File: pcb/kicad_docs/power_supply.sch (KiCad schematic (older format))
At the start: 32 parts, among them J5 power_in, U7 AMS1117-3.3

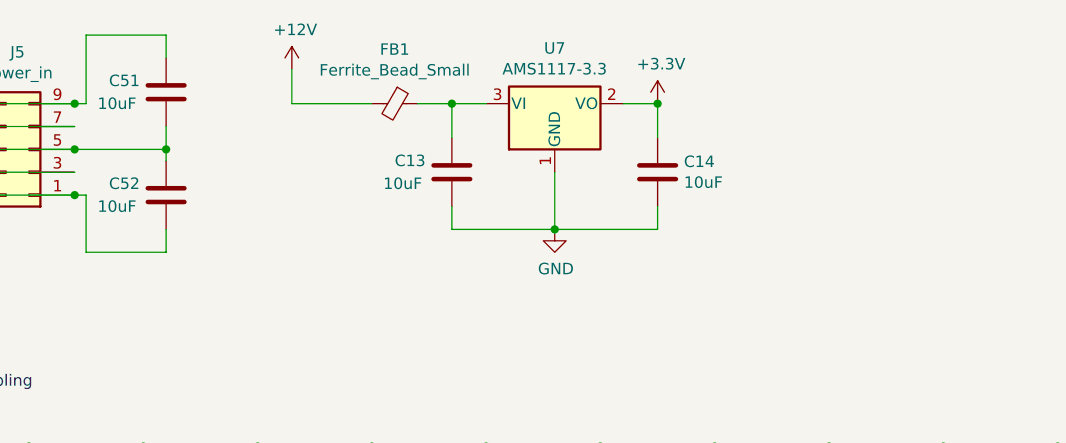
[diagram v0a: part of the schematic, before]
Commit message: add title blocks, fix some erc violations
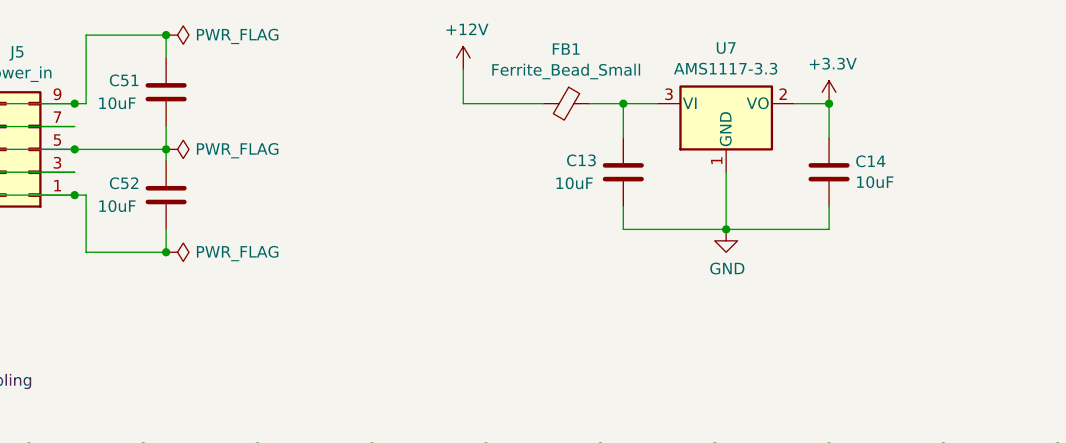
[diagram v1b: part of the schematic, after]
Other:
- moved on the sheet: C13, C14, FB1, U7
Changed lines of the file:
@@
 encoding utf-8
 Sheet 5 10
-Title ""
-Date ""
-Rev ""
+Title "Quad ADSR"
+Date "2020-07-31"
+Rev "0"
 Comp ""
-Comment1 ""
-Comment2 ""
-Comment3 ""
+Comment1 "creativecommons.org/licenses/by/4.0/"
+Comment2 "License: CC by 4.0"
+Comment3 "Author: Jordan Aceto"
 Comment4 ""
 $EndDescr
@@
 L power:GND #PWR045
 U 1 1 5EE07C6F
-P 3800 1550
-F 0 "#PWR045" H 3800 1300 50  0001 C CNN
-F 1 "GND" H 3805 1377 50  0000 C CNN
-F 2 "" H 3800 1550 50  0001 C CNN
-F 3 "" H 3800 1550 50  0001 C CNN
-	1    3800 1550
-	1    0    0    -1
-$EndComp
-Connection ~ 4250 1000
+P 4550 1550
+F 0 "#PWR045" H 4550 1300 50  0001 C CNN
+F 1 "GND" H 4555 1377 50  0000 C CNN
+F 2 "" H 4550 1550 50  0001 C CNN
+F 3 "" H 4550 1550 50  0001 C CNN
+	1    4550 1550
+	1    0    0    -1
+$EndComp
+Connection ~ 5000 1000
 $Comp
 L power:+3.3V #PWR046
 U 1 1 5EE05D61
-P 4250 1000
-F 0 "#PWR046" H 4250 850 50  0001 C CNN
-F 1 "+3.3V" H 4265 1173 50  0000 C CNN
-F 2 "" H 4250 1000 50  0001 C CNN
-F 3 "" H 4250 1000 50  0001 C CNN
-	1    4250 1000
-	1    0    0    -1
-$EndComp
-Wire Wire Line
-	2650 1000 3000 1000
-Wire Wire Line
-	2650 1000 2650 850
+P 5000 1000
+F 0 "#PWR046" H 5000 850 50  0001 C CNN
+F 1 "+3.3V" H 5015 1173 50  0000 C CNN
+F 2 "" H 5000 1000 50  0001 C CNN
+F 3 "" H 5000 1000 50  0001 C CNN
+	1    5000 1000
+	1    0    0    -1
+$EndComp
+Wire Wire Line
+	3400 1000 3750 1000
+Wire Wire Line
+	3400 1000 3400 850
 $Comp
 L power:+12V #PWR044
 U 1 1 5EE0026F
-P 2650 850
-F 0 "#PWR044" H 2650 700 50  0001 C CNN
-F 1 "+12V" H 2665 1023 50  0000 C CNN
-F 2 "" H 2650 850 50  0001 C CNN
-F 3 "" H 2650 850 50  0001 C CNN
-	1    2650 850
-	1    0    0    -1
-$EndComp
-Wire Wire Line
-	3800 1550 4250 1550
-Connection ~ 3800 1550
-Wire Wire Line
-	3800 1300 3800 1550
-Wire Wire Line
-	4250 1550 4250 1450
-Wire Wire Line
-	3350 1550 3800 1550
-Wire Wire Line
-	3350 1450 3350 1550
-Wire Wire Line
-	4250 1000 4100 1000
-Wire Wire Line
-	4250 1150 4250 1000
-Wire Wire Line
-	3350 1000 3500 1000
-Connection ~ 3350 1000
-Wire Wire Line
-	3350 1150 3350 1000
-Wire Wire Line
-	3200 1000 3350 1000
+P 3400 850
+F 0 "#PWR044" H 3400 700 50  0001 C CNN
+F 1 "+12V" H 3415 1023 50  0000 C CNN
+F 2 "" H 3400 850 50  0001 C CNN
+F 3 "" H 3400 850 50  0001 C CNN
+	1    3400 850
+	1    0    0    -1
+$EndComp
+Wire Wire Line
+	4550 1550 5000 1550
+Connection ~ 4550 1550
+Wire Wire Line
+	4550 1300 4550 1550
+Wire Wire Line
+	5000 1550 5000 1450
+Wire Wire Line
+	4100 1550 4550 1550
+Wire Wire Line
+	4100 1450 4100 1550
+Wire Wire Line
+	5000 1000 4850 1000
+Wire Wire Line
+	5000 1150 5000 1000
+Wire Wire Line
+	4100 1000 4250 1000
+Connection ~ 4100 1000
+Wire Wire Line
+	4100 1150 4100 1000
+Wire Wire Line
+	3950 1000 4100 1000
 $Comp
 L Device:Ferrite_Bead_Small FB1
 U 1 1 5EDEC41C
-P 3100 1000
-F 0 "FB1" V 2863 1000 50  0000 C CNN
-F 1 "Ferrite_Bead_Small" V 2954 1000 50  0000 C CNN
-F 2 "Inductor_SMD:L_0805_2012Metric" V 3030 1000 50  0001 C CNN
-F 3 "~" H 3100 1000 50  0001 C CNN
-	1    3100 1000
+P 3850 1000
+F 0 "FB1" V 3613 1000 50  0000 C CNN
+F 1 "Ferrite_Bead_Small" V 3704 1000 50  0000 C CNN
+F 2 "Inductor_SMD:L_0805_2012Metric" V 3780 1000 50  0001 C CNN
+F 3 "~" H 3850 1000 50  0001 C CNN
+	1    3850 1000
 	0    1    1    0
 $EndComp
@@
 L Device:C C14
 U 1 1 5EDEAF58
-P 4250 1300
-F 0 "C14" H 4365 1346 50  0000 L CNN
-F 1 "10uF" H 4365 1255 50  0000 L CNN
-F 2 "Capacitor_SMD:C_0805_2012Metric" H 4288 1150 50  0001 C CNN
-F 3 "~" H 4250 1300 50  0001 C CNN
-	1    4250 1300
+P 5000 1300
+F 0 "C14" H 5115 1346 50  0000 L CNN
+F 1 "10uF" H 5115 1255 50  0000 L CNN
+F 2 "Capacitor_SMD:C_0805_2012Metric" H 5038 1150 50  0001 C CNN
+F 3 "~" H 5000 1300 50  0001 C CNN
+	1    5000 1300
 	1    0    0    -1
 $EndComp
@@
 L Device:C C13
 U 1 1 5EDEA933
-P 3350 1300
-F 0 "C13" H 3100 1350 50  0000 L CNN
-F 1 "10uF" H 3050 1250 50  0000 L CNN
-F 2 "Capacitor_SMD:C_1206_3216Metric" H 3388 1150 50  0001 C CNN
-F 3 "~" H 3350 1300 50  0001 C CNN
-	1    3350 1300
+P 4100 1300
+F 0 "C13" H 3850 1350 50  0000 L CNN
+F 1 "10uF" H 3800 1250 50  0000 L CNN
+F 2 "Capacitor_SMD:C_1206_3216Metric" H 4138 1150 50  0001 C CNN
+F 3 "~" H 4100 1300 50  0001 C CNN
+	1    4100 1300
 	1    0    0    -1
 $EndComp
@@
 L Regulator_Linear:AMS1117-3.3 U7
 U 1 1 5EDEA43C
-P 3800 1000
-F 0 "U7" H 3800 1242 50  0000 C CNN
-F 1 "AMS1117-3.3" H 3800 1151 50  0000 C CNN
-F 2 "Package_TO_SOT_SMD:SOT-223-3_TabPin2" H 3800 1200 50  0001 C CNN
-F 3 "http://www.advanced-monolithic.com/pdf/ds1117.pdf" H 3900 750 50  0001 C CNN
-	1    3800 1000
+P 4550 1000
+F 0 "U7" H 4550 1242 50  0000 C CNN
+F 1 "AMS1117-3.3" H 4550 1151 50  0000 C CNN
+F 2 "Package_TO_SOT_SMD:SOT-223-3_TabPin2" H 4550 1200 50  0001 C CNN
+F 3 "http://www.advanced-monolithic.com/pdf/ds1117.pdf" H 4650 750 50  0001 C CNN
+	1    4550 1000
 	1    0    0    -1
 $EndComp
@@
 Text Notes 900  6650 0    50   ~ 0
 24LCxx EEPROM decoupling
+$Comp
+L power:PWR_FLAG #FLG0101
+U 1 1 5F24F24E
+P 2100 700
+F 0 "#FLG0101" H 2100 775 50  0001 C CNN
+F 1 "PWR_FLAG" V 2100 828 50  0000 L CNN
+F 2 "" H 2100 700 50  0001 C CNN
+F 3 "~" H 2100 700 50  0001 C CNN
+	1    2100 700
+	0    1    1    0
+$EndComp
+Connection ~ 2100 700
+$Comp
+L power:PWR_FLAG #FLG0102
+U 1 1 5F260231
+P 2100 1200
+F 0 "#FLG0102" H 2100 1275 50  0001 C CNN
+F 1 "PWR_FLAG" V 2100 1328 50  0000 L CNN
+F 2 "" H 2100 1200 50  0001 C CNN
+F 3 "~" H 2100 1200 50  0001 C CNN
+	1    2100 1200
+	0    1    1    0
+$EndComp
+$Comp
+L power:PWR_FLAG #FLG0103
+U 1 1 5F2605FC
+P 2100 1650
+F 0 "#FLG0103" H 2100 1725 50  0001 C CNN
+F 1 "PWR_FLAG" V 2100 1778 50  0000 L CNN
+F 2 "" H 2100 1650 50  0001 C CNN
+F 3 "~" H 2100 1650 50  0001 C CNN
+	1    2100 1650
+	0    1    1    0
+$EndComp
+Connection ~ 2100 1650
 $EndSCHEMATC
